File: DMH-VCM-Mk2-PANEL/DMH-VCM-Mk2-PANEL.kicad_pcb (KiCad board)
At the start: 2 copper layers, 50 x 200 mm, 27 parts, among them J0 Panel_GND_Solder_Wire_Pad

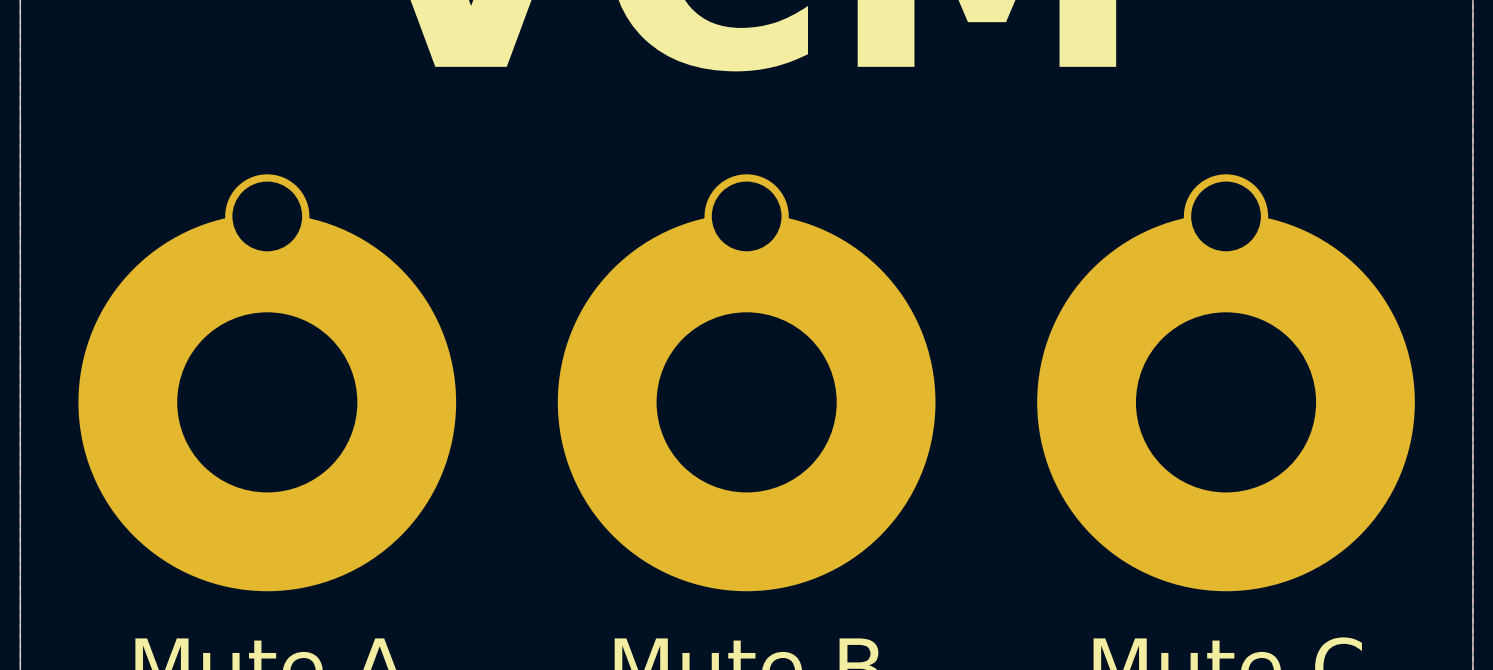
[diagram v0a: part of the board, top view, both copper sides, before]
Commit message: Updated symbols and fps as per library
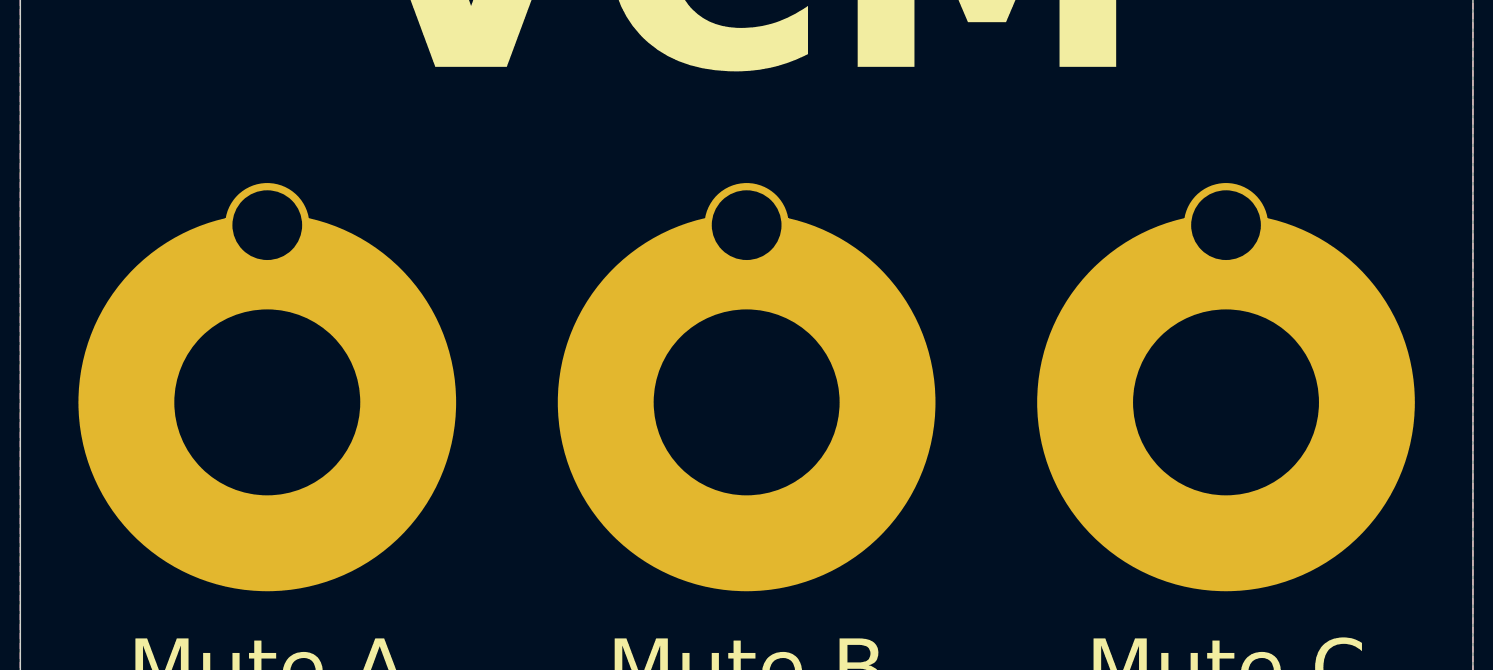
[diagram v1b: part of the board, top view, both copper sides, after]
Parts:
- H19, H20, H21: footprint SynthStuff:Toggle_Switch_Cutout -> SynthStuff:Toggle_Switch_TE_Cutout
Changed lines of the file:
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@@
 		(property ki_fp_filters "Pot_Cutout_*")
 		(sheetname "/")
-		(sheetfile "DMH_Tripple_VCA_PANEL.kicad_sch")
+		(sheetfile "DMH-VCM-Mk2-PANEL.kicad_sch")
 		(attr through_hole exclude_from_bom)
 		(fp_line
@@
 		(property ki_fp_filters "MountingHole*Pad*")
 		(sheetname "/")
-		(sheetfile "DMH_Tripple_VCA_PANEL.kicad_sch")
+		(sheetfile "DMH-VCM-Mk2-PANEL.kicad_sch")
 		(attr exclude_from_pos_files exclude_from_bom)
 		(fp_circle
@@
 		(property ki_fp_filters "Pot_Cutout_*")
 		(sheetname "/")
-		(sheetfile "DMH_Tripple_VCA_PANEL.kicad_sch")
+		(sheetfile "DMH-VCM-Mk2-PANEL.kicad_sch")
 		(attr through_hole exclude_from_bom)
 		(fp_line
@@
 		(property ki_fp_filters "MountingHole*")
 		(sheetname "/")
-		(sheetfile "DMH_Tripple_VCA_PANEL.kicad_sch")
+		(sheetfile "DMH-VCM-Mk2-PANEL.kicad_sch")
 		(attr through_hole exclude_from_bom)
 		(fp_poly
@@
 		(property ki_fp_filters "MountingHole*")
 		(sheetname "/")
-		(sheetfile "DMH_Tripple_VCA_PANEL.kicad_sch")
+		(sheetfile "DMH-VCM-Mk2-PANEL.kicad_sch")
 		(attr exclude_from_pos_files exclude_from_bom)
 		(fp_circle
@@
 		(property ki_fp_filters "MountingHole*")
 		(sheetname "/")
-		(sheetfile "DMH_Tripple_VCA_PANEL.kicad_sch")
+		(sheetfile "DMH-VCM-Mk2-PANEL.kicad_sch")
 		(attr through_hole exclude_from_bom)
 		(fp_poly
@@
 		)
 	)
-	(footprint "SynthStuff:Toggle_Switch_Cutout"
+	(footprint "SynthStuff:Toggle_Switch_TE_Cutout"
 		(layer "F.Cu")
 		(at 75 52)
@@
 		(property ki_fp_filters "MountingHole*")
 		(sheetname "/")
-		(sheetfile "DMH_Tripple_VCA_PANEL.kicad_sch")
+		(sheetfile "DMH-VCM-Mk2-PANEL.kicad_sch")
 		(attr through_hole exclude_from_bom)
 		(fp_circle
@@
 		)
 		(pad "1" thru_hole circle
-			(at 0 -6.4)
+			(at 0 -6.1)
 			(size 2.9 2.9)
 			(drill 2.4)
@@
 			(at 0 0)
 			(size 13 13)
-			(drill 6.2)
+			(drill 6.4)
 			(layers "*.Cu" "*.Mask")
 			(remove_unused_layers no)
@@
 		(property ki_fp_filters "MountingHole*")
 		(sheetname "/")
-		(sheetfile "DMH_Tripple_VCA_PANEL.kicad_sch")
+		(sheetfile "DMH-VCM-Mk2-PANEL.kicad_sch")
 		(attr through_hole exclude_from_bom)
 		(fp_circle
@@
 		(property ki_fp_filters "MountingHole*")
 		(sheetname "/")
-		(sheetfile "DMH_Tripple_VCA_PANEL.kicad_sch")
+		(sheetfile "DMH-VCM-Mk2-PANEL.kicad_sch")
 		(attr exclude_from_pos_files exclude_from_bom)
 		(fp_circle
@@
 		(property ki_fp_filters "Pot_Cutout_*")
 		(sheetname "/")
-		(sheetfile "DMH_Tripple_VCA_PANEL.kicad_sch")
+		(sheetfile "DMH-VCM-Mk2-PANEL.kicad_sch")
 		(attr through_hole exclude_from_bom)
 		(fp_line
@@
 		(property ki_fp_filters "MountingHole*")
 		(sheetname "/")
-		(sheetfile "DMH_Tripple_VCA_PANEL.kicad_sch")
+		(sheetfile "DMH-VCM-Mk2-PANEL.kicad_sch")
 		(attr exclude_from_pos_files exclude_from_bom)
 		(fp_circle
@@
 		(property ki_fp_filters "MountingHole*")
 		(sheetname "/")
-		(sheetfile "DMH_Tripple_VCA_PANEL.kicad_sch")
+		(sheetfile "DMH-VCM-Mk2-PANEL.kicad_sch")
 		(attr through_hole exclude_from_bom)
 		(fp_poly
@@
 		(property ki_fp_filters "Pot_Cutout_*")
 		(sheetname "/")
-		(sheetfile "DMH_Tripple_VCA_PANEL.kicad_sch")
+		(sheetfile "DMH-VCM-Mk2-PANEL.kicad_sch")
 		(attr through_hole exclude_from_bom)
 		(fp_line
@@
 		(property ki_fp_filters "MountingHole*")
 		(sheetname "/")
-		(sheetfile "DMH_Tripple_VCA_PANEL.kicad_sch")
+		(sheetfile "DMH-VCM-Mk2-PANEL.kicad_sch")
 		(attr through_hole exclude_from_bom)
 		(fp_circle
@@
 		(property ki_fp_filters "MountingHole*")
 		(sheetname "/")
-		(sheetfile "DMH_Tripple_VCA_PANEL.kicad_sch")
+		(sheetfile "DMH-VCM-Mk2-PANEL.kicad_sch")
 		(attr through_hole exclude_from_bom)
 		(fp_circle
@@
 		(property ki_fp_filters "MountingHole*")
 		(sheetname "/")
-		(sheetfile "DMH_Tripple_VCA_PANEL.kicad_sch")
+		(sheetfile "DMH-VCM-Mk2-PANEL.kicad_sch")
 		(attr through_hole exclude_from_bom)
 		(fp_circle
@@
 		(property ki_fp_filters "Pot_Cutout_*")
 		(sheetname "/")
-		(sheetfile "DMH_Tripple_VCA_PANEL.kicad_sch")
+		(sheetfile "DMH-VCM-Mk2-PANEL.kicad_sch")
 		(attr through_hole exclude_from_bom)
 		(fp_line
@@
 		)
 	)
-	(footprint "SynthStuff:Toggle_Switch_Cutout"
+	(footprint "SynthStuff:Toggle_Switch_TE_Cutout"
 		(layer "F.Cu")
 		(at 91.5 52)
@@
 		(property ki_fp_filters "MountingHole*")
 		(sheetname "/")
-		(sheetfile "DMH_Tripple_VCA_PANEL.kicad_sch")
+		(sheetfile "DMH-VCM-Mk2-PANEL.kicad_sch")
 		(attr through_hole exclude_from_bom)
 		(fp_circle
@@
 		)
 		(pad "1" thru_hole circle
-			(at 0 -6.4)
+			(at 0 -6.1)
 			(size 2.9 2.9)
 			(drill 2.4)
@@
 			(at 0 0)
 			(size 13 13)
-			(drill 6.2)
+			(drill 6.4)
 			(layers "*.Cu" "*.Mask")
 			(remove_unused_layers no)
@@
 		(property ki_fp_filters "MountingHole*Pad*")
 		(sheetname "/")
-		(sheetfile "DMH_Tripple_VCA_PANEL.kicad_sch")
+		(sheetfile "DMH-VCM-Mk2-PANEL.kicad_sch")
 		(attr exclude_from_pos_files exclude_from_bom)
 		(fp_circle
@@
 		(property ki_fp_filters "MountingHole*Pad*")
 		(sheetname "/")
-		(sheetfile "DMH_Tripple_VCA_PANEL.kicad_sch")
+		(sheetfile "DMH-VCM-Mk2-PANEL.kicad_sch")
 		(attr exclude_from_pos_files exclude_from_bom)
 		(fp_circle
@@
 		(property ki_fp_filters "MountingHole*Pad*")
 		(sheetname "/")
-		(sheetfile "DMH_Tripple_VCA_PANEL.kicad_sch")
+		(sheetfile "DMH-VCM-Mk2-PANEL.kicad_sch")
 		(attr exclude_from_pos_files exclude_from_bom)
 		(fp_circle
@@
 		(embedded_fonts no)
 	)
-	(footprint "SynthStuff:Toggle_Switch_Cutout"
+	(footprint "SynthStuff:Toggle_Switch_TE_Cutout"
 		(layer "F.Cu")
 		(at 58.5 52)
@@
 		(property ki_fp_filters "MountingHole*")
 		(sheetname "/")
-		(sheetfile "DMH_Tripple_VCA_PANEL.kicad_sch")
+		(sheetfile "DMH-VCM-Mk2-PANEL.kicad_sch")
 		(attr through_hole exclude_from_bom)
 		(fp_circle
@@
 		)
 		(pad "1" thru_hole circle
-			(at 0 -6.4)
+			(at 0 -6.1)
 			(size 2.9 2.9)
 			(drill 2.4)
@@
 			(at 0 0)
 			(size 13 13)
-			(drill 6.2)
+			(drill 6.4)
 			(layers "*.Cu" "*.Mask")
 			(remove_unused_layers no)
@@
 		(property ki_fp_filters "Pot_Cutout_*")
 		(sheetname "/")
-		(sheetfile "DMH_Tripple_VCA_PANEL.kicad_sch")
+		(sheetfile "DMH-VCM-Mk2-PANEL.kicad_sch")
 		(attr through_hole exclude_from_bom)
 		(fp_line
@@
 		(property ki_fp_filters "MountingHole*")
 		(sheetname "/")
-		(sheetfile "DMH_Tripple_VCA_PANEL.kicad_sch")
+		(sheetfile "DMH-VCM-Mk2-PANEL.kicad_sch")
 		(attr through_hole exclude_from_bom)
 		(fp_circle
@@
 		(property ki_fp_filters "MountingHole*")
 		(sheetname "/")
-		(sheetfile "DMH_Tripple_VCA_PANEL.kicad_sch")
+		(sheetfile "DMH-VCM-Mk2-PANEL.kicad_sch")
 		(attr through_hole exclude_from_bom)
 		(fp_poly
@@
 		(property ki_fp_filters "MountingHole*")
 		(sheetname "/")
-		(sheetfile "DMH_Tripple_VCA_PANEL.kicad_sch")
+		(sheetfile "DMH-VCM-Mk2-PANEL.kicad_sch")
 		(attr through_hole exclude_from_bom)
 		(fp_circle
@@
 		(property ki_fp_filters "Connector*:*_1x??_*")
 		(sheetname "/")
-		(sheetfile "DMH_Tripple_VCA_PANEL.kicad_sch")
+		(sheetfile "DMH-VCM-Mk2-PANEL.kicad_sch")
 		(zone_connect 1)
 		(attr smd exclude_from_pos_files exclude_from_bom)

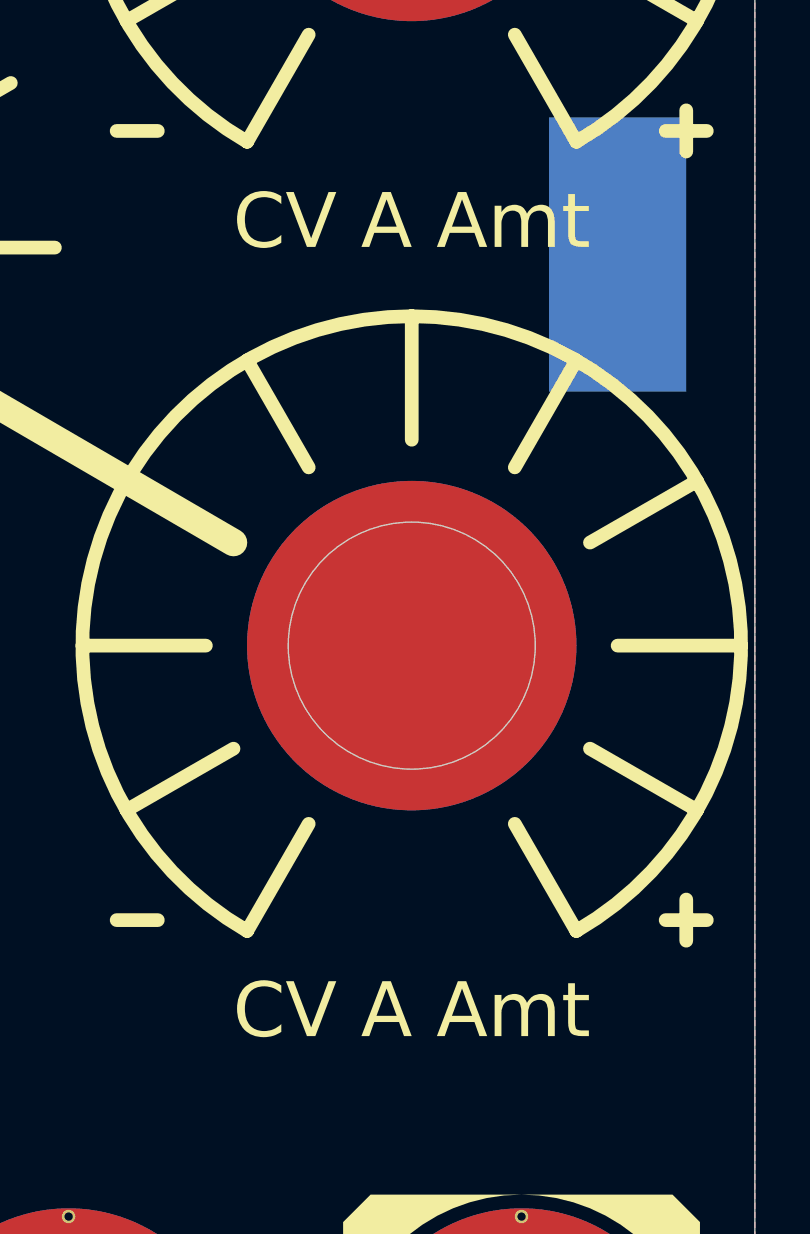
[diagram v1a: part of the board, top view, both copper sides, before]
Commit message: Almost finished PCB 1 schematic
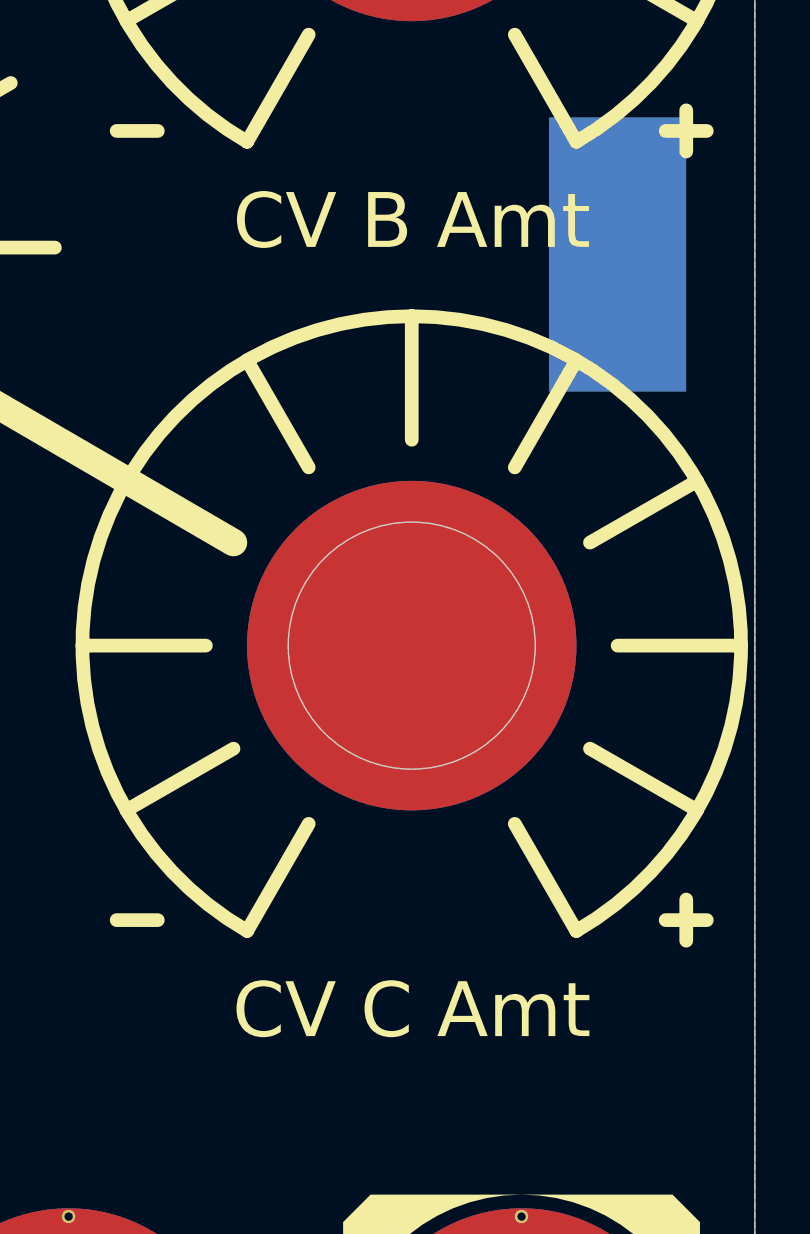
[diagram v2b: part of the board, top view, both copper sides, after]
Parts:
- H25: value CV A Amt -> CV B Amt
- H26: value CV A Amt -> CV C Amt

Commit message: Generated Gerbers
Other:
- board text added: "Mk2.0 - October 2025"
- board text removed: "Mk2.0 - Mxxxx 2025"

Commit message: Kicad 10 and updated SynthStuff
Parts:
- H17, H22, H23: footprint SynthStuff:MountingHole_LED_3mm -> SynthStuff:MountingHole_LED_3mm_R
